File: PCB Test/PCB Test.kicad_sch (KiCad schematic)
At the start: 47 parts, among them J1 Motor Terminal 2, J5 Motor Terminal 1, J6 Conn_02x03_Odd_Even, Q2 NMOS, Q3 NMOS, SW1 SW_Push, SW2 SW_Push, SW3 SW_Push, U1 ATmega4808-A, U2 TCRT5000, U3 TCRT5000, U4 TCRT5000, U5 MCP1700x-330xxTO

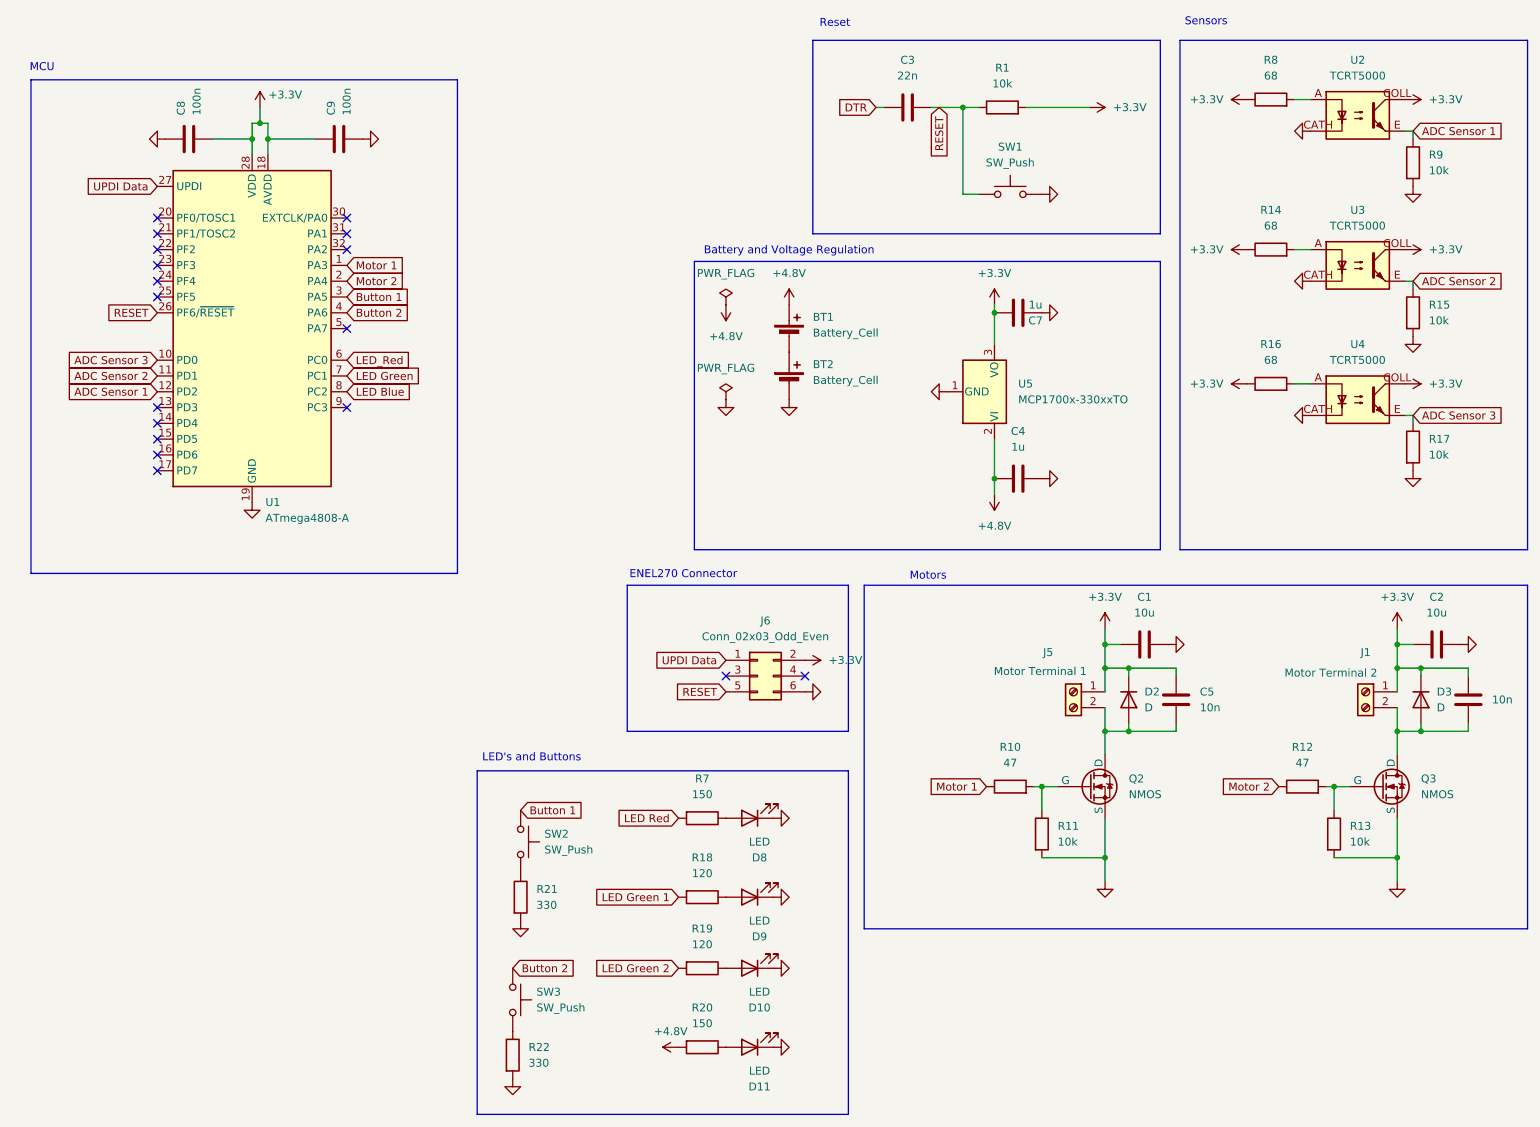
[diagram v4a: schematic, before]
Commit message: Started on the PCB Layout, added ENEL270 programming pin, fixed motor voltages
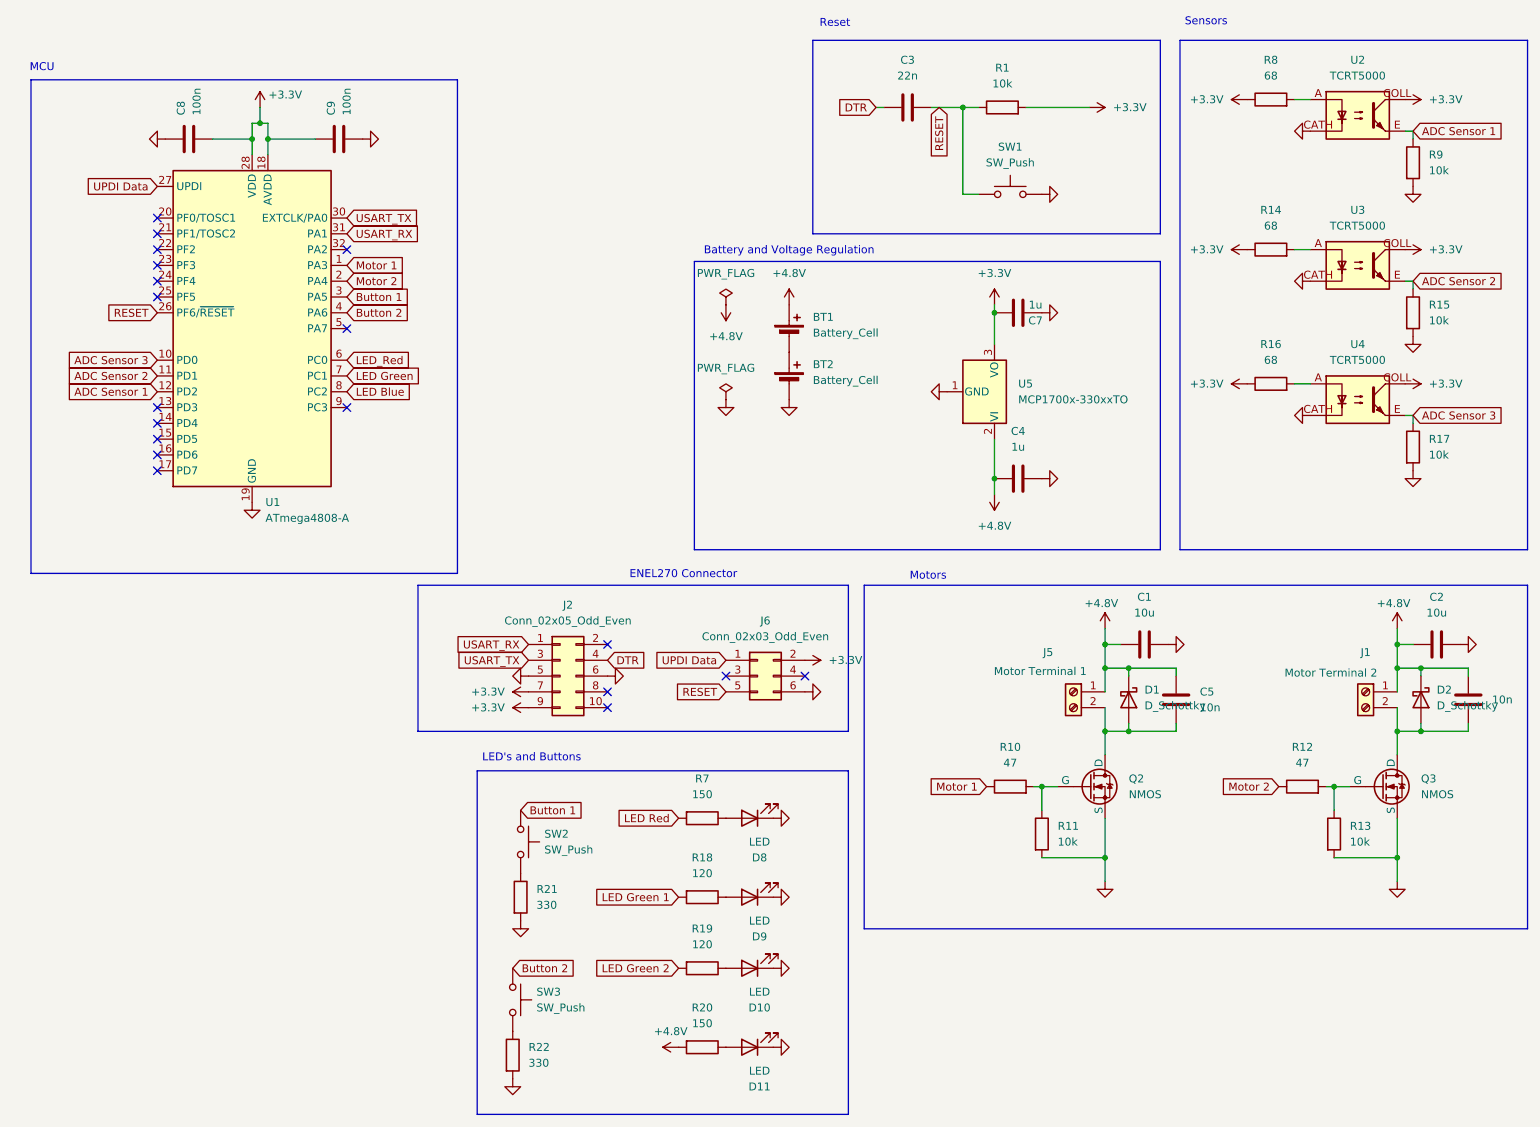
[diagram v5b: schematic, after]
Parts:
- removed D2, D3: D, FBY8:P30_D7.3x22, symbol Device:D
- added D1, D2: D_Schottky, Diode_SMD:D_SMA, symbol Device:D_Schottky
- added J2: Conn_02x05_Odd_Even, Connector_PinSocket_1.00mm:PinSocket_2x05_P1.00mm_Vertical_SMD, symbol Connector_Generic:Conn_02x05_Odd_Even
- J6: footprint Connector:Tag-Connect_TC2030-IDC-FP_2x03_P1.27mm_Vertical -> Connector_PinSocket_1.00mm:PinSocket_2x03_P1.00mm_Vertical_SMD
- Q2, Q3: footprint Package_TO_SOT_SMD:SC-59_Handsoldering -> Package_TO_SOT_SMD:SOT-23
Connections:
- net +3.3V: now also J2.7 (Pin_7), J2.9 (Pin_9); no longer C1.2, C2.2, C5.1, C6.1, J1.1 (Pin_1), J5.1 (Pin_1)
- net +4.8V: now also C1.2, C2.2, C5.1, C6.1, J1.1 (Pin_1), J5.1 (Pin_1), D1.1 (K), D2.1 (K)
- net DTR: now also J2.4 (Pin_4)
- net GND: now also J2.5 (Pin_5), J2.6 (Pin_6)
- net at C6.2, J1.2 (Pin_2), Q3.1 (D): now also D2.2 (A)
- net at C5.2, J5.2 (Pin_2), Q2.1 (D): now also D1.2 (A)
- net USART_TX: now reaches U1.30 (EXTCLK/PA0)
- net USART_TX: now also J2.3 (Pin_3)
- net USART_RX: now reaches U1.31 (PA1)
- net USART_RX: now also J2.1 (Pin_1)
- no-connect marks 18 -> 19

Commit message: I think finished a rough layout
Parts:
- U2, U3, U4: footprint OptoDevice:Vishay_TCRT5000 -> Connector_Harwin:Harwin_LTek-Male_2x02_P2.00mm_Vertical
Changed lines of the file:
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@@
 	(wire
 		(pts
-			(xy 218.44 119.38) (xy 215.9 119.38)
-		)
-		(stroke
-			(width 0)
-			(type default)
-		)
-	)
-	(wire
-		(pts
 			(xy 266.7 123.19) (xy 274.32 123.19)
 		)
@@
 	(wire
 		(pts
+			(xy 215.9 119.38) (xy 218.44 119.38)
+		)
+		(stroke
+			(width 0)
+			(type default)
+		)
+	)
+	(wire
+		(pts
 			(xy 215.9 157.48) (xy 215.9 153.67)
 		)
@@
 			)
 		)
-		(property "Footprint" "OptoDevice:Vishay_TCRT5000"
+		(property "Footprint" "Connector_Harwin:Harwin_LTek-Male_2x02_P2.00mm_Vertical"
 			(at 256.54 42.545 0)
 			(hide yes)
@@
 			)
 		)
-		(property "Footprint" "OptoDevice:Vishay_TCRT5000"
+		(property "Footprint" "Connector_Harwin:Harwin_LTek-Male_2x02_P2.00mm_Vertical"
 			(at 256.54 66.675 0)
 			(hide yes)
@@
 			)
 		)
-		(property "Footprint" "OptoDevice:Vishay_TCRT5000"
+		(property "Footprint" "Connector_Harwin:Harwin_LTek-Male_2x02_P2.00mm_Vertical"
 			(at 256.54 88.265 0)
 			(hide yes)

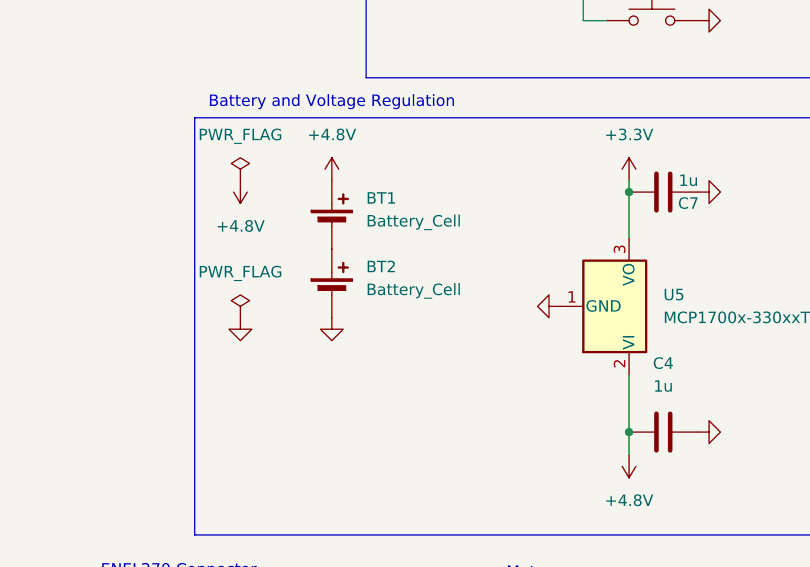
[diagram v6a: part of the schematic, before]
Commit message: Restructured the board, added a battery connector
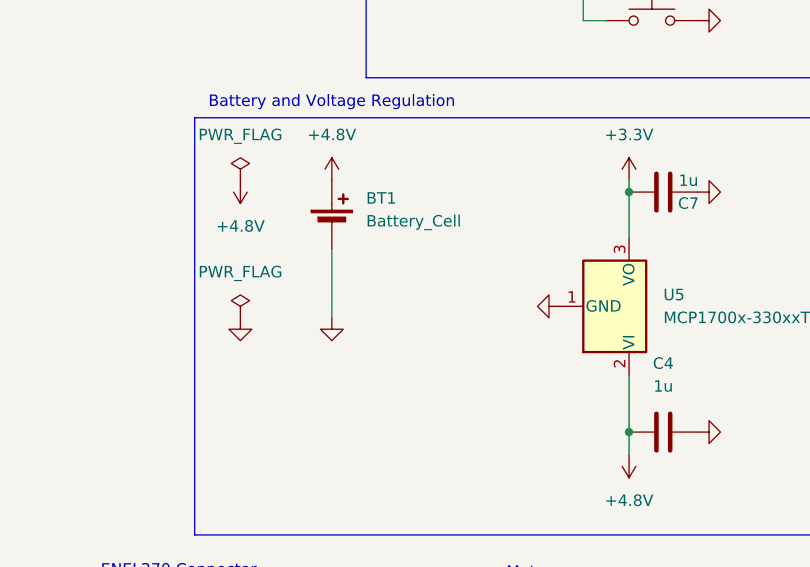
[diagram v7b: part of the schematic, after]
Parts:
- removed BT2: Battery_Cell, Battery:BatteryHolder_Keystone_2462_2xAA, symbol Device:Battery_Cell
- BT1: footprint Battery:BatteryHolder_Keystone_2462_2xAA -> Connector_PinSocket_1.00mm:PinSocket_1x02_P1.00mm_Vertical_SMD_Pin1Left
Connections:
- net GND: now also BT1.2 (-)
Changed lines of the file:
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@@
 	(wire
 		(pts
+			(xy 165.1 72.39) (xy 165.1 80.01)
+		)
+		(stroke
+			(width 0)
+			(type default)
+		)
+	)
+	(wire
+		(pts
 			(xy 262.89 133.35) (xy 266.7 133.35)
 		)
@@
 			)
 		)
-		(property "Footprint" "Battery:BatteryHolder_Keystone_2462_2xAA"
+		(property "Footprint" "Connector_PinSocket_1.00mm:PinSocket_1x02_P1.00mm_Vertical_SMD_Pin1Left"
 			(at 165.1 68.326 90)
 			(hide yes)
@@
 					(unit 1)
 				)
-			)
-		)
-	)
-	(symbol
-		(lib_id "Device:Battery_Cell")
-		(at 165.1 77.47 0)
-		(unit 1)
-		(body_style 1)
-		(exclude_from_sim no)
-		(in_bom yes)
-		(on_board yes)
-		(in_pos_files yes)
-		(dnp no)
-		(fields_autoplaced yes)
-		(property "Reference" "BT2"
-			(at 168.91 74.3584 0)
-			(show_name no)
-			(do_not_autoplace no)
-			(effects
-				(font
-					(size 1.27 1.27)
-				)
-				(justify left)
-			)
-		)
-		(property "Value" "Battery_Cell"
-			(at 168.91 76.8984 0)
-			(show_name no)
-			(do_not_autoplace no)
-			(effects
-				(font
-					(size 1.27 1.27)
-				)
-				(justify left)
-			)
-		)
-		(property "Footprint" "Battery:BatteryHolder_Keystone_2462_2xAA"
-			(at 165.1 75.946 90)
-			(hide yes)
-			(show_name no)
-			(do_not_autoplace no)
-			(effects
-				(font
-					(size 1.27 1.27)
-				)
-			)
-		)
-		(property "Datasheet" ""
-			(at 165.1 75.946 90)
-			(hide yes)
-			(show_name no)
-			(do_not_autoplace no)
-			(effects
-				(font
-					(size 1.27 1.27)
-				)
-			)
-		)
-		(property "Description" "Single-cell battery"
-			(at 165.1 77.47 0)
-			(hide yes)
-			(show_name no)
-			(do_not_autoplace no)
-			(effects
-				(font
-					(size 1.27 1.27)
-				)
-			)
-		)
-		(property "Sim.Device" "V"
-			(at 165.1 77.47 0)
-			(hide yes)
-			(show_name no)
-			(do_not_autoplace no)
-			(effects
-				(font
-					(size 1.27 1.27)
-				)
-			)
-		)
-		(property "Sim.Type" "DC"
-			(at 165.1 77.47 0)
-			(hide yes)
-			(show_name no)
-			(do_not_autoplace no)
-			(effects
-				(font
-					(size 1.27 1.27)
-				)
-			)
-		)
-		(property "Sim.Pins" "1=+ 2=-"
-			(at 165.1 77.47 0)
-			(hide yes)
-			(show_name no)
-			(do_not_autoplace no)
-			(effects
-				(font
-					(size 1.27 1.27)
-				)
-			)
-		)
-		(pin "1"
-		)
-		(pin "2"
-		)
-		(instances
-			(project "PCB Test"
-				(path "/7fcd8b9a-e9e6-4d51-9258-8399f733a0d2"
-					(reference "BT2")
-					(unit 1)
-				)

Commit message: Final layout finished, moving on to motion transmition, need to extract gerber files
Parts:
- removed J1: Motor Terminal 2, TerminalBlock:TerminalBlock_MaiXu_MX126-5.0-02P_1x02_P5.00mm, symbol Connector:Screw_Terminal_01x02
- removed J5: Motor Terminal 1, TerminalBlock:TerminalBlock_MaiXu_MX126-5.0-02P_1x02_P5.00mm, symbol Connector:Screw_Terminal_01x02
- removed U2, U3, U4: TCRT5000, Connector_Harwin:Harwin_LTek-Male_2x02_P2.00mm_Vertical, symbol tcrt5000:TCRT5000
- added H1, H2, H3, H4: MountingHole, MountingHole:MountingHole_2.2mm_M2, symbol Mechanical:MountingHole
- added J1: Conn_02x02_Counter_Clockwise, Connector:NS-Tech_Grove_1x04_P2mm_Vertical, symbol Connector_Generic:Conn_02x02_Counter_Clockwise
- added J3, J4, J5: Conn_02x02_Odd_Even, Connector_Harwin:Harwin_LTek-Male_2x02_P2.00mm_Vertical, symbol Connector_Generic:Conn_02x02_Odd_Even
- J2: footprint Connector_PinSocket_1.00mm:PinSocket_2x05_P1.00mm_Vertical_SMD -> Connector_PinHeader_1.00mm:PinHeader_2x05_P1.00mm_Vertical_SMD
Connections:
- net LED Blue is gone; now on net LED Green 2: U1.8 (PC2)
- net LED Green is gone; now on net LED Green 1: U1.7 (PC1)
- net LED_Red is gone; now on net LED Red: U1.6 (PC0)
- net +3.3V: now also J3.2 (Pin_2), J4.2 (Pin_2), J5.2 (Pin_2)
- net +4.8V: now also J1.1 (Pin_1), J1.4 (Pin_4)
- net ADC Sensor 1: now also R17.1, J5.4 (Pin_4); no longer R9.1
- net ADC Sensor 2: now also J4.4 (Pin_4)
- net ADC Sensor 3: now also R9.1, J3.4 (Pin_4); no longer R17.1
- net GND: now also J3.3 (Pin_3), J4.3 (Pin_3), J5.3 (Pin_3)
- net Motor 1: now also R12.1; no longer R10.1
- net Motor 2: now also R10.1; no longer R12.1
- net at C5.2, D1.2 (A), Q2.1 (D): now also J1.2 (Pin_2)
- net at R8.2: now also J3.1 (Pin_1)
- net at R14.2: now also J4.1 (Pin_1)
- net at C6.2, D2.2 (A), Q3.1 (D): now also J1.3 (Pin_3)
- net at R16.2: now also J5.1 (Pin_1)
- net USART_RX renamed USART RX
- net USART_TX renamed USART TX
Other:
- note added: "Battery, Voltage Regulation, Mounting Holes"
- note removed: "Battery and Voltage Regulation"
- moved on the sheet: C1, C5, D1, Q2, R10, R11
